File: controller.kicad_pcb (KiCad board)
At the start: 2 copper layers, 57.2 x 38.1 mm, 22 parts, among them M1 VAL**, M2 VAL**, M4 VAL**, P1 CONN_2, P2 CONN_2, P3 CONN_2, Q1 Q_NPN_EBC, SW1 SWITCH_INV, U1 LTC6992_TSOT_32_6, U2 POLOLU_3V3

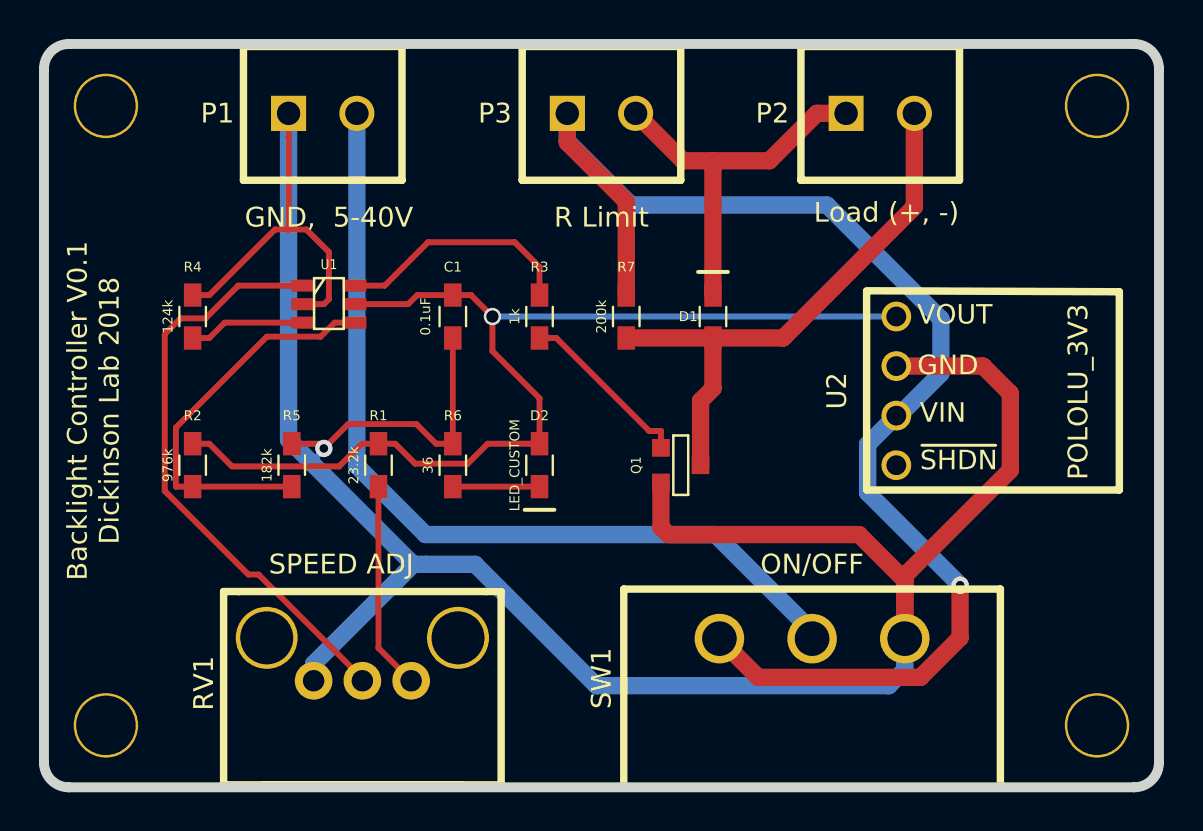
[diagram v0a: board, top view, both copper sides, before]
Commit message: Modified to add external 0-1V analog input control. Made .zip archive of gerber files.
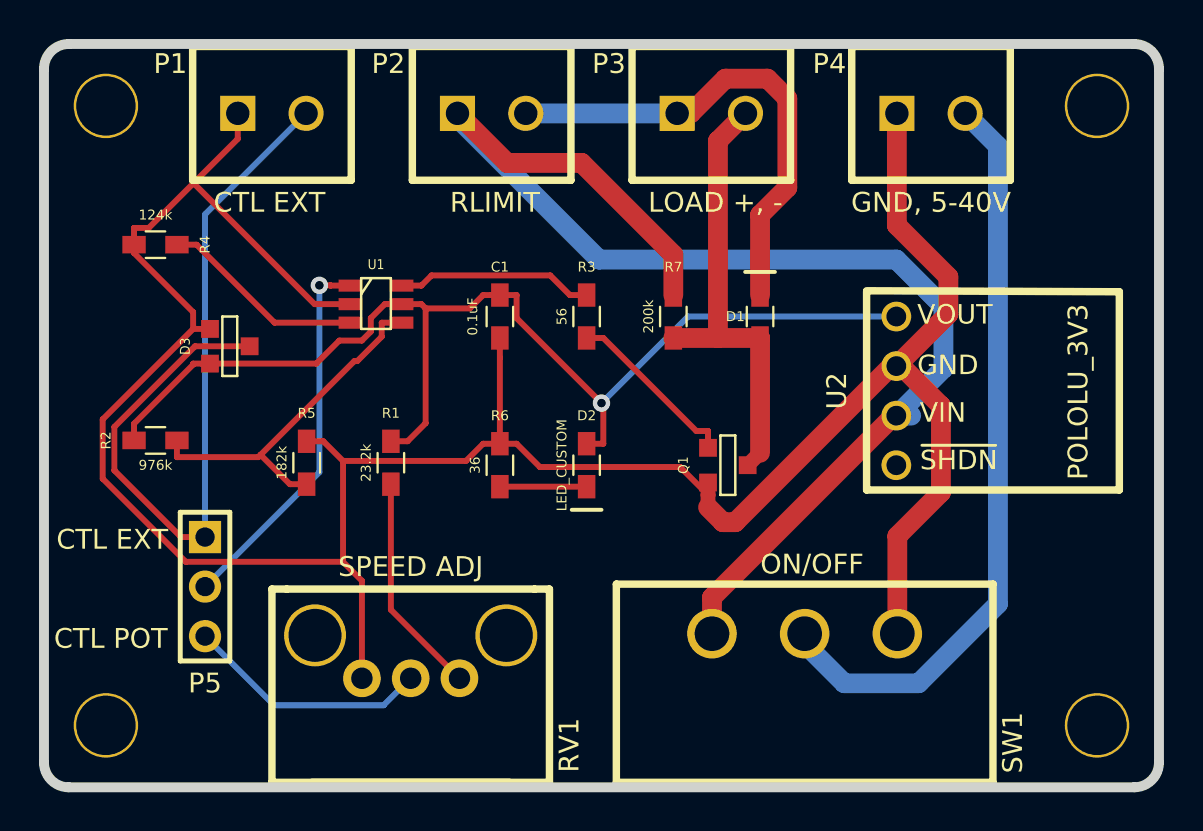
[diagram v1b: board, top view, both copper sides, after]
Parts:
- added D3: BAS07-04, BAS07:SOT23EBC, F.Cu at (33.9, 40.9)
- added P4: CONN_2, BLOCK_CONN_2:BLOCK_CONN_2X1, F.Cu at (70.9, 29.0)
- added P5: CONN_3, PIN_ARRAY_1X3:PIN_ARRAY_1X3, F.Cu at (33.7, 53.2)
- R3: value 1k -> 56
- moved P2 19.9 mm to (48.3, 29.0)
- moved P3 5.63 mm to (59.6, 29.0)
- moved R4 4.15 mm to (31.1, 35.7), turned to 180 degrees
- moved P1 2.60 mm to (37.1, 29.0)
- moved RV1 2.48 mm to (44.2, 57.9)
- moved C1 2.41 mm to (48.8, 39.4)
- moved D1 2.41 mm to (62.1, 39.4)
- moved D2 2.41 mm to (53.2, 47.0)
- moved R3 2.41 mm to (53.2, 39.4)
- moved R6 2.41 mm to (48.8, 47.0)
- moved R7 2.41 mm to (57.7, 39.4)
- moved Q1 2.41 mm to (60.5, 47.0)
- moved U1 2.41 mm to (42.4, 38.7)
- moved R2 2.29 mm to (31.1, 45.7), turned to 0 degrees
- moved R5 0.77 mm to (38.9, 46.9)
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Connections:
- P1 pad 2: Net-(P1-Pad2) -> Net-(D3-Pad3)
- P2 pad 1: Net-(D1-Pad2) -> /VIN
- P2 pad 2: Net-(D1-Pad1) -> Net-(D1-Pad2)
- P3 pad 1: /VIN -> Net-(D1-Pad2)
- P3 pad 2: Net-(D1-Pad2) -> Net-(D1-Pad1)
- RV1 pad 2: Net-(RV1-Pad2) -> Net-(P5-Pad3)
- SW1 pad 2: Net-(P1-Pad2) -> Net-(P4-Pad2)
- U1 pad 1: Net-(RV1-Pad2) -> Net-(P5-Pad2)
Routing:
- net Net-(P1-Pad2): track 46.1 -> 0.00 mm
- net Net-(D3-Pad3): track 0.00 -> 40.8 mm
- net Net-(P4-Pad2): track 0.00 -> 38.8 mm
- net Net-(RV1-Pad2): track 30.4 -> 0.00 mm
- net Net-(P5-Pad2): track 0.00 -> 19.5 mm, vias 0 -> 1
- net Net-(P5-Pad3): track 0.00 -> 12.6 mm
- net Net-(D1-Pad1): track 29.1 -> 23.3 mm
- net Net-(D1-Pad2): track 19.7 -> 25.2 mm
- net Net-(R4-Pad1): track 6.00 -> 10.5 mm
- net /3V3: track 55.5 -> 59.3 mm
- net GND: track 138.2 -> 135.0 mm, vias 1 -> 0
- net Net-(R3-Pad2): track 12.4 -> 10.1 mm
- net Net-(R2-Pad2): track 20.3 -> 18.6 mm
- net /VIN: track 68.8 -> 67.9 mm, vias 1 -> 0
- net Net-(R1-Pad2): track 10.6 -> 11.4 mm
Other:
- net class Power: trace_width 0.889 -> 1.016
- board text added: "CTL EXT"
- board text added: "CTL POT"
- board text added: "LOAD +, -"
- board text added: "RLIMIT"
- board text removed: "Load (+, -)"
- board text removed: "R Limit"
